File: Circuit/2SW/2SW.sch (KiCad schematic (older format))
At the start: 30 parts, among them IC1 PIC16F18857-I_SP, J1 Conn_01x14_Female, J2 Conn_01x14_Female, J3 S8B-XH-A-1_LF__SN_, J4 S8B-XH-A-1_LF__SN_, U1 MAX485E

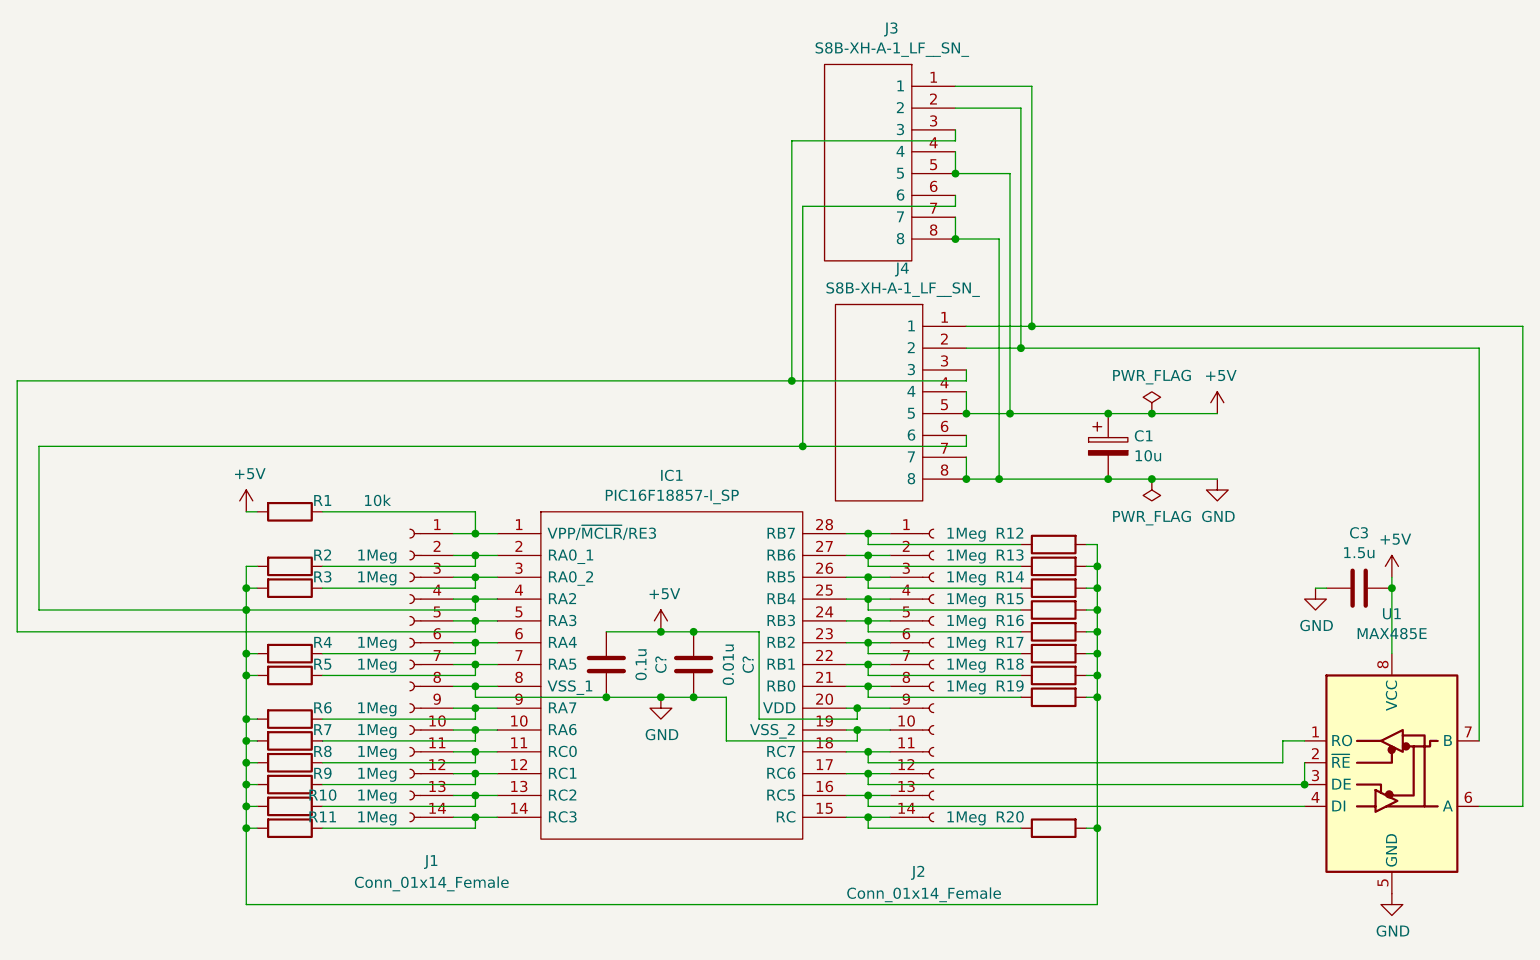
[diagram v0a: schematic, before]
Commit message: 8bit circuit (chip#0-5) complete
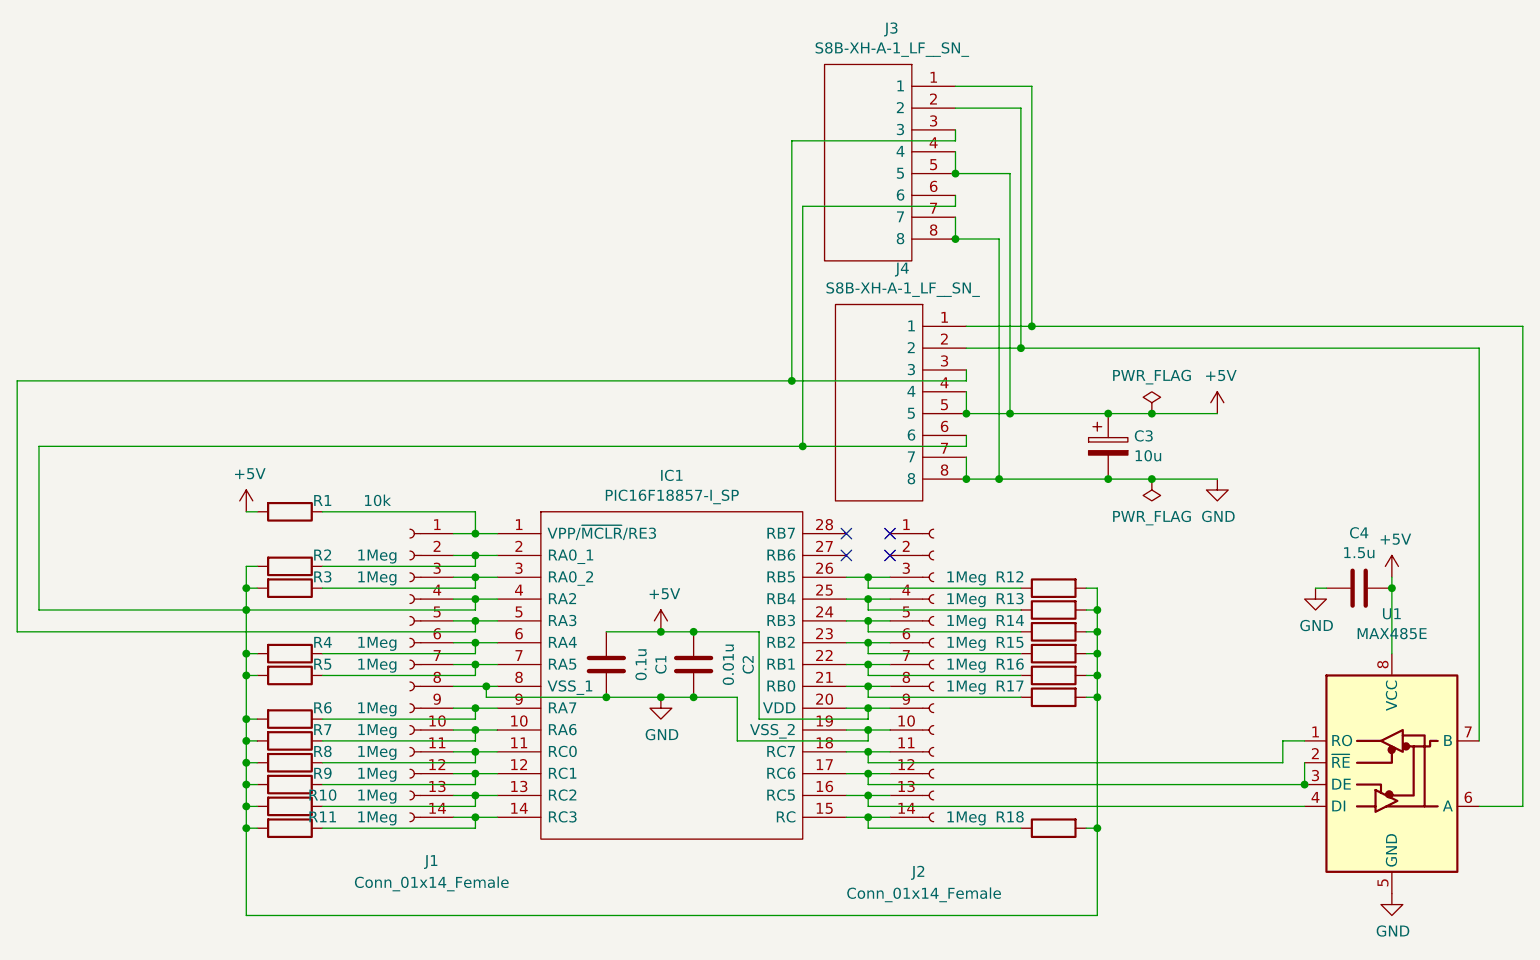
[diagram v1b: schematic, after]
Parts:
- removed C?: 0.1u, symbol Device:C
- removed C?: 0.01u, symbol Device:C
- removed R12, R13: 1Meg, symbol Device:R
- added C1: 0.1u, symbol Device:C
- added C2: 0.01u, symbol Device:C
- renumbered C1 to C3, C3 to C4, R14 to R12, R15 to R13, R16 to R14, R17 to R15, R18 to R16, R19 to R17, R20 to R18
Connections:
- net +5V: now also C1.2, C2.2
- net GND: now also C1.1, C2.1
- net at IC1.27 (RB6): no longer J2.2 (Pin_2)
- net at IC1.28 (RB7): no longer J2.1 (Pin_1)
- no-connect marks 0 -> 4
